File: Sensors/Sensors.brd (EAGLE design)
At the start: 101.6 x 53.3 mm, 36 parts, among them J2 JST_CONNECTOR, J6 JST_CONNECTOR, J7 JST_CONNECTOR, J8 JST_CONNECTOR, J9 JST_CONNECTOR

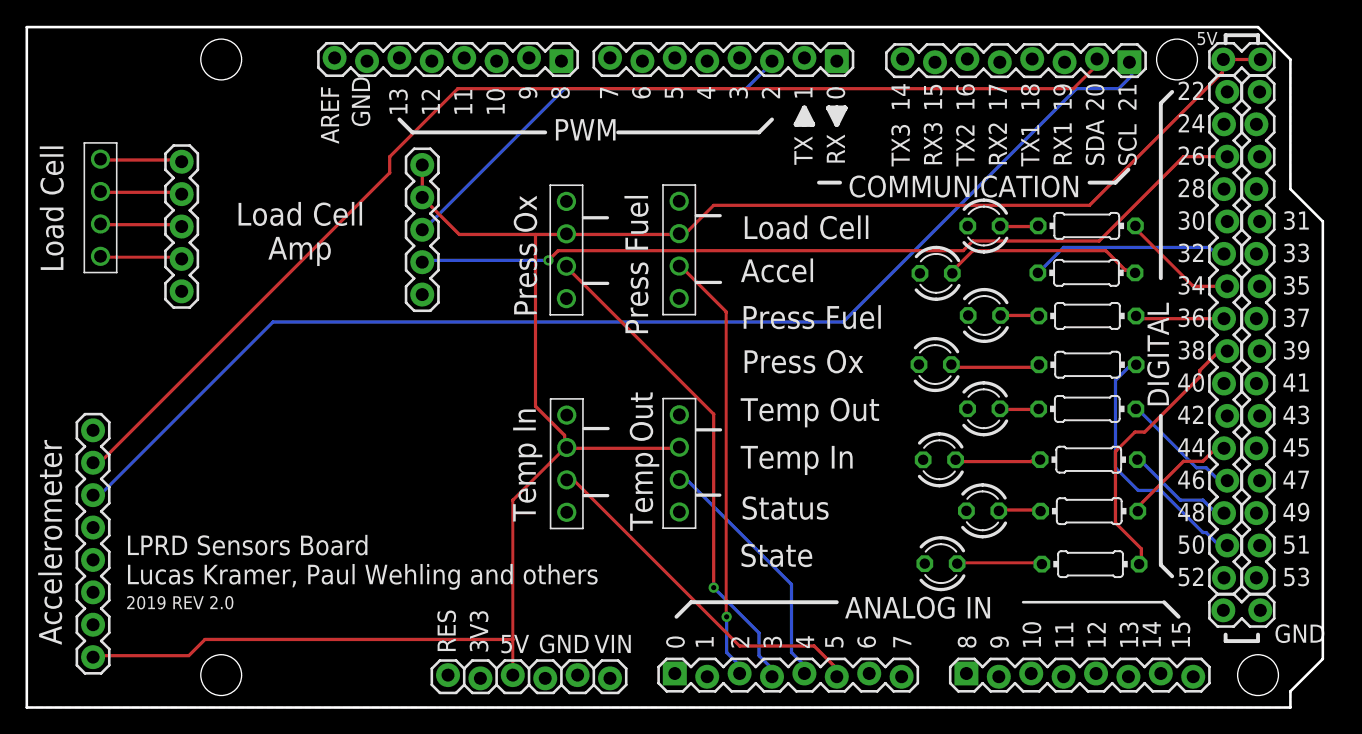
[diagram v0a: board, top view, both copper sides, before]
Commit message: Fix mistakes in sensors schematic
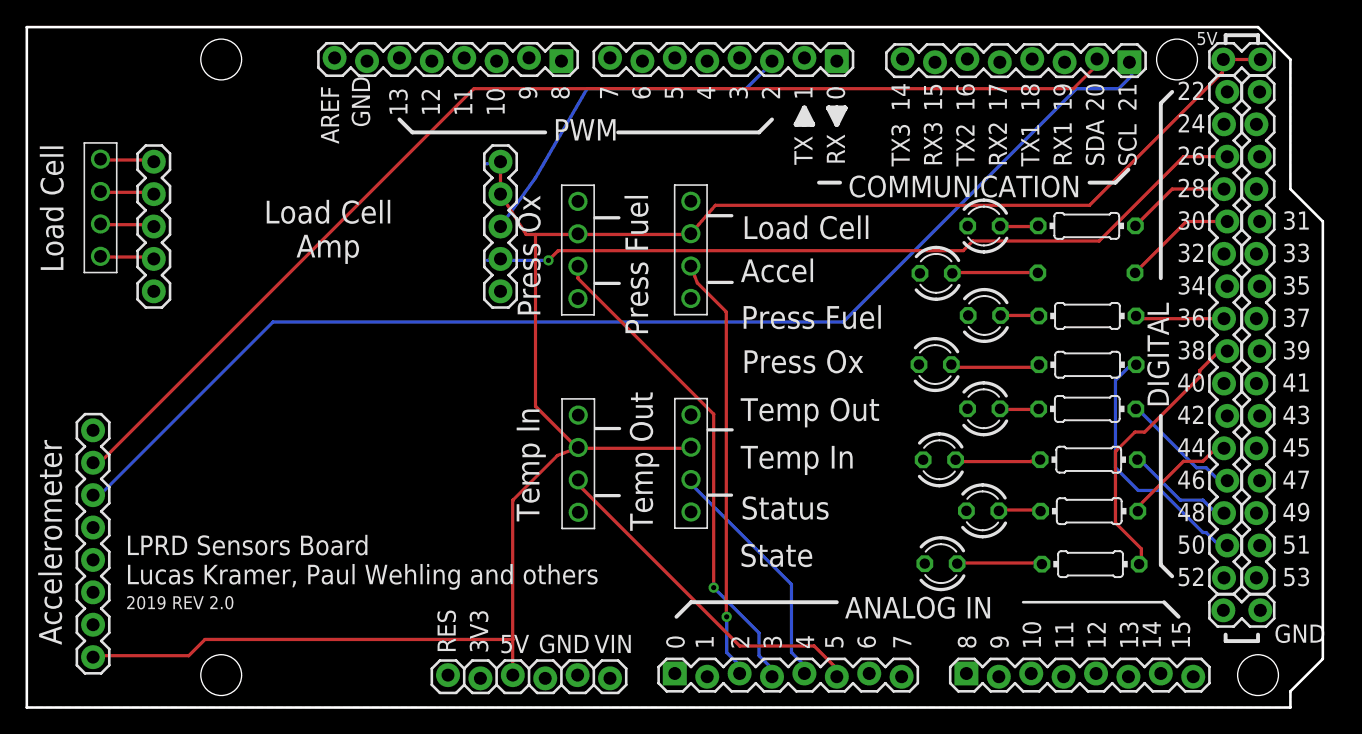
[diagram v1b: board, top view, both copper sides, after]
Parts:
- moved J4 6.14 mm to (37.1, 32.6)
- moved J3 2.18 mm to (9.96, 32.6)
- moved J6 0.91 mm to (52.1, 20.4)
- moved J8 0.91 mm to (52.1, 37.1)
- moved J7 0.90 mm to (43.2, 20.4)
- moved J9 0.90 mm to (43.2, 37.1)
- flipped R1 to the bottom
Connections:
- net D50 renamed D24
- removed net D44: JP9.12
- removed net D46: JP9.13
- new net D40: JP9.7
- new net D42: JP9.6
- net ACCEL_LED: now also JP9.12; no longer JP9.11
- net D22: now also JP9.16; no longer JP9.1
- net D23: now also JP8.1; no longer JP8.16
- net D25: now also JP8.2; no longer JP8.15
- net D27: now also JP8.3; no longer JP8.14
- net D29: now also JP8.4; no longer JP8.13
- net D31: now also JP8.5; no longer JP8.12
- net D32: now also JP9.11; no longer JP9.6
- net D33: now also JP8.6; no longer JP8.11
- net D34: now also JP9.10; no longer JP9.7
- net D35: now also JP8.7; no longer JP8.10
- net D37: now also JP8.8; no longer JP8.9
- net D39: now also JP8.9; no longer JP8.8
- net D41: now also JP8.10; no longer JP8.7
- net D43: now also JP8.11; no longer JP8.6
- net D45: now also JP8.12; no longer JP8.5
- net D47: now also JP8.13; no longer JP8.4
- net D49: now also JP8.14; no longer JP8.3
- net D51: now also JP8.15; no longer JP8.2
- net D52: now also JP9.1; no longer JP9.16
- net D53: now also JP8.16; no longer JP8.1
- net FORCE_LED: now also JP9.13; no longer JP9.10
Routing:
- net N$1: track 16.0 -> 6.78 mm
- net ACCEL_LED: track 15.6 -> 8.89 mm
- net FORCE_DAT: track 32.9 -> 28.2 mm
- net FORCE_CLK: track 66.5 -> 62.3 mm
- net 5V: track 155.6 -> 152.9 mm
- net E-/BLACK: track 6.43 -> 4.22 mm
- net E+/RED: track 6.43 -> 4.22 mm
- net A-/WHITE: track 6.43 -> 4.22 mm
- net A+/GREEN: track 6.43 -> 4.22 mm
- net FORCE_LED: track 9.30 -> 8.14 mm
- net SDA: track 92.8 -> 92.1 mm
- net VOUT_PRESSURE_FUEL: track 33.9 -> 33.4 mm

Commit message: Fix net naming error
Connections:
- net VOUT_PRESSURE_FUEL: now also J9.P$2, JP7.4; no longer J8.P$2, JP7.3
- net VOUT_PRESSURE_OX: now also J8.P$2, JP7.3; no longer J9.P$2, JP7.4
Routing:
- net VOUT_PRESSURE_OX: track 38.5 -> 33.4 mm
- net VOUT_PRESSURE_FUEL: track 33.4 -> 38.5 mm
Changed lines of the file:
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@@
 <contactref element="J3" pad="1"/>
 </signal>
-<signal name="VOUT_PRESSURE_OX">
+<signal name="VOUT_PRESSURE_FUEL">
 <contactref element="JP7" pad="4"/>
 <contactref element="J9" pad="P$2"/>
@@
 <via x="53.848" y="9.398" extent="1-16" drill="0.4064"/>
 </signal>
-<signal name="VOUT_PRESSURE_FUEL">
+<signal name="VOUT_PRESSURE_OX">
 <contactref element="JP7" pad="3"/>
 <contactref element="J8" pad="P$2"/>
